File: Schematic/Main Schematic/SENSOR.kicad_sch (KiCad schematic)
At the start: 11 parts, among them IC1 LM75AD,118

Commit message: Updated main schematic but not entirely
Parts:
- renumbered C1 to C9, R1 to R7, R4 to R8, R5 to R9
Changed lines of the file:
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@@
   (symbol (lib_id "power:GND") (at 110.6932 129.2606 0) (unit 1)
     (in_bom yes) (on_board yes) (dnp no) (fields_autoplaced)
-    (property "Reference" "#PWR08" (at 110.6932 135.6106 0)
+    (property "Reference" "#PWR011" (at 110.6932 135.6106 0)
       (effects (font (size 1.27 1.27)) hide)
     )
@@
   (symbol (lib_id "power:GND") (at 87.8332 100.0506 270) (unit 1)
     (in_bom yes) (on_board yes) (dnp no) (fields_autoplaced)
-    (property "Reference" "#PWR05" (at 81.4832 100.0506 0)
+    (property "Reference" "#PWR010" (at 81.4832 100.0506 0)
       (effects (font (size 1.27 1.27)) hide)
     )
@@
   (symbol (lib_id "Device:R") (at 78.9432 109.5756 0) (unit 1)
     (in_bom yes) (on_board yes) (dnp no) (fields_autoplaced)
-    (property "Reference" "R5" (at 81.026 108.9406 0)
+    (property "Reference" "R9" (at 81.026 108.9406 0)
       (effects (font (size 1.27 1.27)) (justify left))
     )
@@
   (symbol (lib_id "power:+3V3") (at 113.1824 92.4306 0) (unit 1)
     (in_bom yes) (on_board yes) (dnp no) (fields_autoplaced)
-    (property "Reference" "#PWR09" (at 113.1824 96.2406 0)
+    (property "Reference" "#PWR012" (at 113.1824 96.2406 0)
       (effects (font (size 1.27 1.27)) hide)
     )
@@
   (symbol (lib_id "Device:R") (at 70.0532 109.5756 0) (unit 1)
     (in_bom yes) (on_board yes) (dnp no) (fields_autoplaced)
-    (property "Reference" "R4" (at 72.5932 108.3055 0)
+    (property "Reference" "R8" (at 72.5932 108.3055 0)
       (effects (font (size 1.27 1.27)) (justify left))
     )
@@
   (symbol (lib_id "Device:R") (at 62.4332 109.5756 0) (unit 1)
     (in_bom yes) (on_board yes) (dnp no) (fields_autoplaced)
-    (property "Reference" "R1" (at 64.9732 108.3055 0)
+    (property "Reference" "R7" (at 64.9732 108.3055 0)
       (effects (font (size 1.27 1.27)) (justify left))
     )
@@
   (symbol (lib_id "pspice:CAP") (at 104.3432 100.0506 90) (unit 1)
     (in_bom yes) (on_board yes) (dnp no) (fields_autoplaced)
-    (property "Reference" "C1" (at 104.3432 91.1606 90)
+    (property "Reference" "C9" (at 104.3432 91.1606 90)
       (effects (font (size 1.27 1.27)))
     )
@@
   (symbol (lib_id "power:GND") (at 85.2932 134.3406 0) (unit 1)
     (in_bom yes) (on_board yes) (dnp no) (fields_autoplaced)
-    (property "Reference" "#PWR01" (at 85.2932 140.6906 0)
-      (effects (font (size 1.27 1.27)) hide)
-    )
+    (property "Reference" "#PWR09" (at 85.2932 140.6906 0)
+      (effects (font (size 1.27 1.27)) hide)
+    )

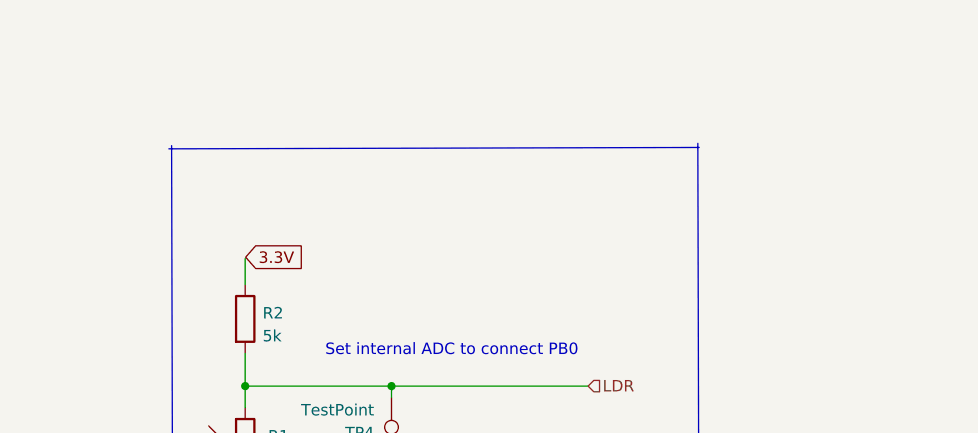
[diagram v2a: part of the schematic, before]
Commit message: I made few comments on the sensing
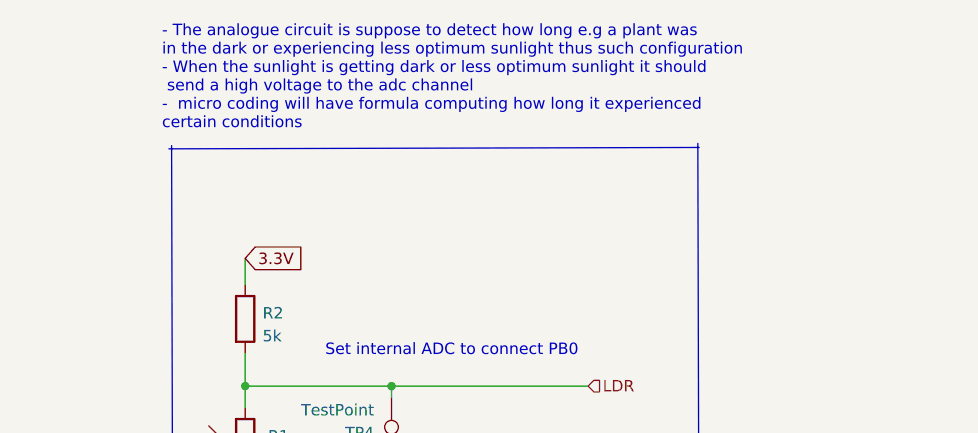
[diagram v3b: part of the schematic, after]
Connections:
- net 3.3V: now also R2.1
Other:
- note added: "- The analogue circuit is suppose to detect how long e.g a plant was in the dark or experiencing less optimum sunlight thus such configuration - When the sunlight is getting dark or less optimum sunlight it should send a high voltage to the adc channel - micro coding will have formula computing how long it experienced certain conditions"
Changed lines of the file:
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@@
     (stroke (width 0) (type default))
+  )
+  (text "- The analogue circuit is suppose to detect how long e.g a plant was \nin the dark or experiencing less optimum sunlight thus such configuration\n- When the sunlight is getting dark or less optimum sunlight it should\n send a high voltage to the adc channel\n-  micro coding will have formula computing how long it experienced \ncertain conditions\n"
+    (at 154.94 83.0072 0)
+    (effects (font (size 1.27 1.27)) (justify left bottom))
   )
   (text "Set internal ADC to connect PB0\n\n" (at 173.0756 110.2614 0)
@@
     (effects (font (size 1.27 1.27)) (justify left bottom))
   )
-  (global_label "3.3V" (shape input) (at 164.2364 97.0534 0)
+  (global_label "3.3V" (shape input) (at 164.1856 97.1804 0)
     (effects (font (size 1.27 1.27)) (justify left))
-    (property "Intersheetrefs" "${INTERSHEET_REFS}" (at 164.2364 97.0534 0)
+    (property "Intersheetrefs" "${INTERSHEET_REFS}" (at 164.1856 97.1804 0)
       (effects (font (size 1.27 1.27)) hide)
     )

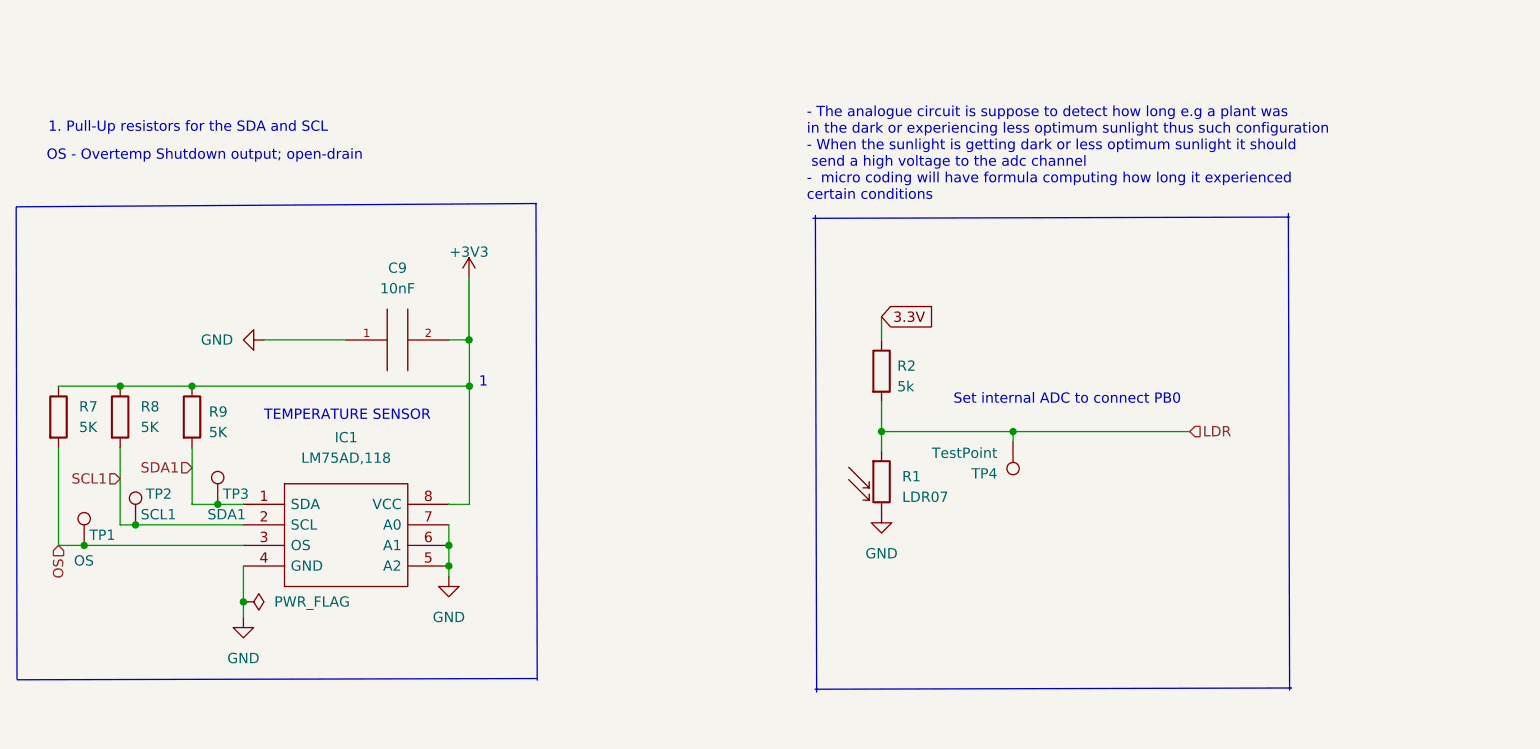
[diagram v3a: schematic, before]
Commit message: I have commented on my module explaining the significant parts
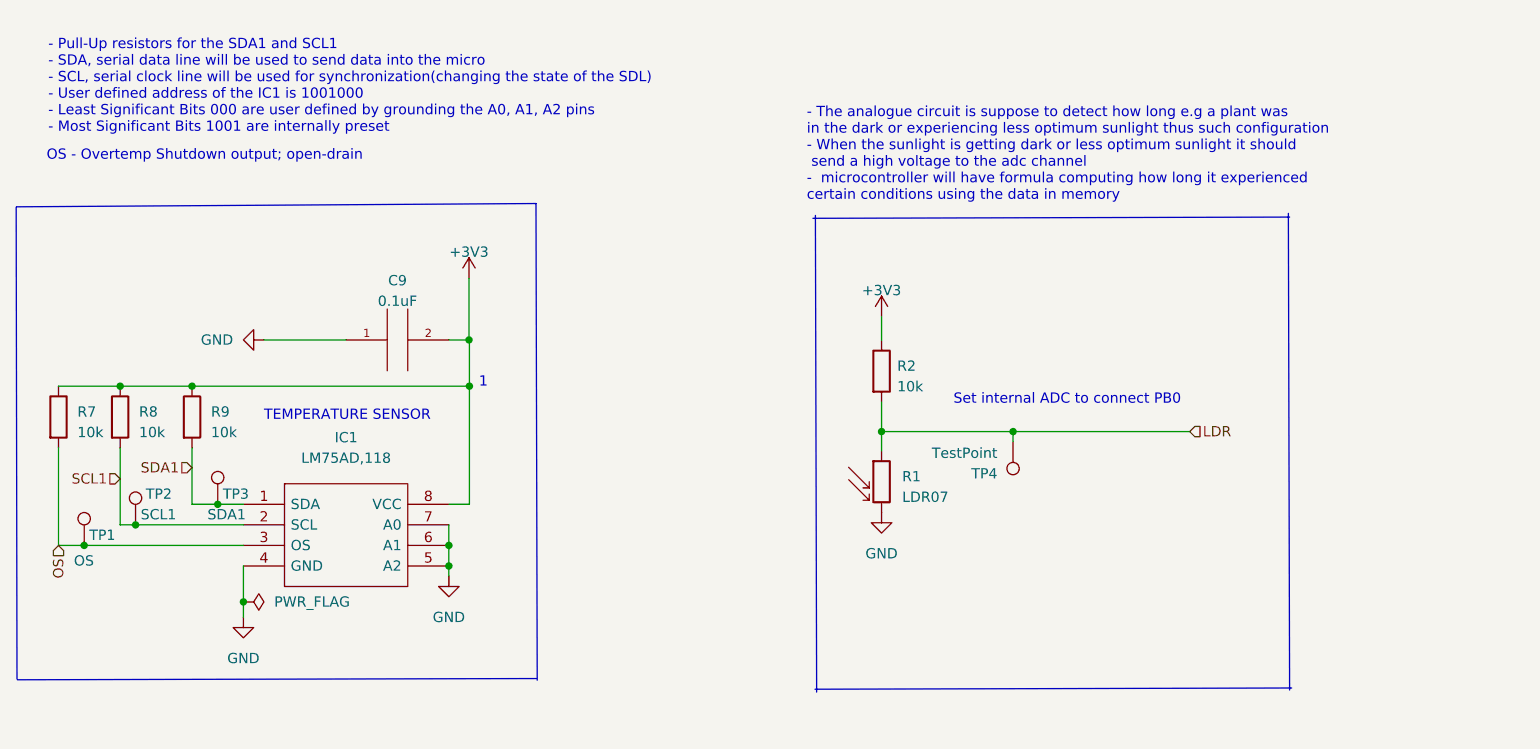
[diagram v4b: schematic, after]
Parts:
- C9: value 10nF -> 0.1uF
- R2: value 5k -> 10k
- R7, R8, R9: value 5K -> 10k
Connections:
- net 3.3V is gone; now on net +3V3: R2.1
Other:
- note added: "- Pull-Up resistors for the SDA1 and SCL1 - SDA, serial data line will be used to send data into the micro - SCL, serial clock line will be used for synchronization(changing the state of the SDL) - User defined address of the IC1 is 1001000 - Least Significant Bits 000 are user defined by grounding the A0, A1, A2 pins - Most Significant Bits 1001 are internally preset"
- note added: "- The analogue circuit is suppose to detect how long e.g a plant was in the dark or experiencing less optimum sunlight thus such configuration - When the sunlight is getting dark or less optimum sunlight it should send a high voltage to the adc channel - microcontroller will have formula computing how long it experienced certain conditions using the data in memory"
- note removed: "- The analogue circuit is suppose to detect how long e.g a plant was in the dark or experiencing less optimum sunlight thus such configuration - When the sunlight is getting dark or less optimum sunlight it should send a high voltage to the adc channel - micro coding will have formula computing how long it experienced certain conditions"
- note removed: "1. Pull-Up resistors for the SDA and SCL"
- company: (none) -> UCT
- title: (none) -> Sensors
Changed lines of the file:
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@@
 (kicad_sch (version 20230121) (generator eeschema)
   (paper "A4")
+  (title_block
+    (title "Sensors")
+    (company "UCT")
+    (comment 4 "Author: Zwivhuya Ndou")
+  )
   (junction (at 164.1856 111.379) (diameter 0) (color 0 0 0 0)
   )
@@
     (stroke (width 0) (type default))
   )
-  (text "- The analogue circuit is suppose to detect how long e.g a plant was \nin the dark or experiencing less optimum sunlight thus such configuration\n- When the sunlight is getting dark or less optimum sunlight it should\n send a high voltage to the adc channel\n-  micro coding will have formula computing how long it experienced \ncertain conditions\n"
+  (text "- The analogue circuit is suppose to detect how long e.g a plant was \nin the dark or experiencing less optimum sunlight thus such configuration\n- When the sunlight is getting dark or less optimum sunlight it should\n send a high voltage to the adc channel\n-  microcontroller will have formula computing how long it experienced \ncertain conditions using the data in memory\n"
     (at 154.94 83.0072 0)
     (effects (font (size 1.27 1.27)) (justify left bottom))
@@
     (effects (font (size 1.27 1.27)) (justify left bottom))
   )
-  (text "1. Pull-Up resistors for the SDA and SCL" (at 61.1632 74.5998 0)
+  (text "- Pull-Up resistors for the SDA1 and SCL1\n- SDA, serial data line will be used to send data into the micro\n- SCL, serial clock line will be used for synchronization(changing the state of the SDL)\n- User defined address of the IC1 is 1001000\n- Least Significant Bits 000 are user defined by grounding the A0, A1, A2 pins\n- Most Significant Bits 1001 are internally preset"
+    (at 61.1632 74.5998 0)
     (effects (font (size 1.27 1.27)) (justify left bottom))
-  )
-  (global_label "3.3V" (shape input) (at 164.1856 97.1804 0)
-    (effects (font (size 1.27 1.27)) (justify left))
-    (property "Intersheetrefs" "${INTERSHEET_REFS}" (at 164.1856 97.1804 0)
-      (effects (font (size 1.27 1.27)) hide)
-    )
   )
   (hierarchical_label "LDR" (shape input) (at 202.2856 111.379 0) (fields_autoplaced)
@@
   (symbol (lib_id "Device:R") (at 78.9432 109.5756 0) (unit 1)
     (in_bom yes) (on_board yes) (dnp no) (fields_autoplaced)
-    (property "Reference" "R9" (at 81.026 108.9406 0)
-      (effects (font (size 1.27 1.27)) (justify left))
-    )
-    (property "Value" "5K" (at 81.026 111.4806 0)
+    (property "Reference" "R9" (at 81.28 108.9406 0)
+      (effects (font (size 1.27 1.27)) (justify left))
+    )
+    (property "Value" "10k" (at 81.28 111.4806 0)
       (effects (font (size 1.27 1.27)) (justify left))
     )
@@
   (symbol (lib_id "Device:R") (at 70.0532 109.5756 0) (unit 1)
     (in_bom yes) (on_board yes) (dnp no) (fields_autoplaced)
-    (property "Reference" "R8" (at 72.5932 108.3055 0)
-      (effects (font (size 1.27 1.27)) (justify left))
-    )
-    (property "Value" "5K" (at 72.5932 110.8455 0)
+    (property "Reference" "R8" (at 72.39 108.9406 0)
+      (effects (font (size 1.27 1.27)) (justify left))
+    )
+    (property "Value" "10k" (at 72.39 111.4806 0)
       (effects (font (size 1.27 1.27)) (justify left))
     )
@@
       (effects (font (size 1.27 1.27)) (justify left))
     )
-    (property "Value" "5k" (at 166.116 105.8164 0)
+    (property "Value" "10k" (at 166.116 105.8164 0)
       (effects (font (size 1.27 1.27)) (justify left))
     )
@@
     )
   )
+  (symbol (lib_id "power:+3V3") (at 164.1856 97.1804 0) (unit 1)
+    (in_bom yes) (on_board yes) (dnp no) (fields_autoplaced)
+    (property "Reference" "#PWR014" (at 164.1856 100.9904 0)
+      (effects (font (size 1.27 1.27)) hide)
+    )
+    (property "Value" "+3V3" (at 164.1856 93.9292 0)
+      (effects (font (size 1.27 1.27)))
+    )
+    (property "Footprint" "" (at 164.1856 97.1804 0)
+      (effects (font (size 1.27 1.27)) hide)
+    )
+    (property "Datasheet" "" (at 164.1856 97.1804 0)
+      (effects (font (size 1.27 1.27)) hide)
+    )
+    (pin "1")
+    (instances
+      (project "Main Schematic"
+        (path "/81c41bad-bb43-41af-b405-18d135a809b1/820a1ce6-42c1-4792-8ad0-5e2a5c074ed4"
+          (reference "#PWR014") (unit 1)
+        )
+      )
+    )
+  )
   (symbol (lib_id "power:GND") (at 164.1856 121.3866 0) (unit 1)
     (in_bom yes) (on_board yes) (dnp no) (fields_autoplaced)
@@
   (symbol (lib_id "Device:R") (at 62.4332 109.5756 0) (unit 1)
     (in_bom yes) (on_board yes) (dnp no) (fields_autoplaced)
-    (property "Reference" "R7" (at 64.9732 108.3055 0)
-      (effects (font (size 1.27 1.27)) (justify left))
-    )
-    (property "Value" "5K" (at 64.9732 110.8455 0)
+    (property "Reference" "R7" (at 64.77 108.9406 0)
+      (effects (font (size 1.27 1.27)) (justify left))
+    )
+    (property "Value" "10k" (at 64.77 111.4806 0)
       (effects (font (size 1.27 1.27)) (justify left))
     )
@@
   (symbol (lib_id "pspice:CAP") (at 104.3432 100.0506 90) (unit 1)
     (in_bom yes) (on_board yes) (dnp no) (fields_autoplaced)
-    (property "Reference" "C9" (at 104.3432 91.1606 90)
-      (effects (font (size 1.27 1.27)))
-    )
-    (property "Value" "10nF" (at 104.3432 93.7006 90)
-      (effects (font (size 1.27 1.27)))
-    )
+    (property "Reference" "C9" (at 104.3432 92.71 90)
+      (effects (font (size 1.27 1.27)))
+    )
+    (property "Value" "0.1uF" (at 104.3432 95.25 90)
+      (effects (font (size 1.27 1.27)))
+    )

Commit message: Sensor comment
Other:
- note added: "- Pull-Up resistors for the SDA1 and SCL1 - SDA, serial data line will be used to send data into the micro - SCL, serial clock line will be used for synchronization(changing the state of the SDL) - User defined address of the IC1 is 1001000 - Least Significant Bits 000 are user defined by grounding the A0, A1, A2 pins - Most Significant Bits 1001 are internally preset - OS - Overtemp Shutdown out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"
- note removed: "- Pull-Up resistors for the SDA1 and SCL1 - SDA, serial data line will be used to send data into the micro - SCL, serial clock line will be used for synchronization(changing the state of the SDL) - User defined address of the IC1 is 1001000 - Least Significant Bits 000 are user defined by grounding the A0, A1, A2 pins - Most Significant Bits 1001 are internally preset"
- note removed: "OS - Overtemp Shutdown output; open-drain"
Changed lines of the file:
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@@
     (effects (font (size 1.27 1.27)) (justify left bottom))
   )
-  (text "OS - Overtemp Shutdown output; open-drain" (at 60.96 78.0542 0)
-    (effects (font (size 1.27 1.27)) (justify left bottom))
-  )
-  (text "- Pull-Up resistors for the SDA1 and SCL1\n- SDA, serial data line will be used to send data into the micro\n- SCL, serial clock line will be used for synchronization(changing the state of the SDL)\n- User defined address of the IC1 is 1001000\n- Least Significant Bits 000 are user defined by grounding the A0, A1, A2 pins\n- Most Significant Bits 1001 are internally preset"
+  (text "- Pull-Up resistors for the SDA1 and SCL1\n- SDA, serial data line will be used to send data into the micro\n- SCL, serial clock line will be used for synchronization(changing the state of the SDL)\n- User defined address of the IC1 is 1001000\n- Least Significant Bits 000 are user defined by grounding the A0, A1, A2 pins\n- Most Significant Bits 1001 are internally preset\n- OS - Overtemp Shutdown output; open-drain"
     (at 61.1632 74.5998 0)
     (effects (font (size 1.27 1.27)) (justify left bottom))

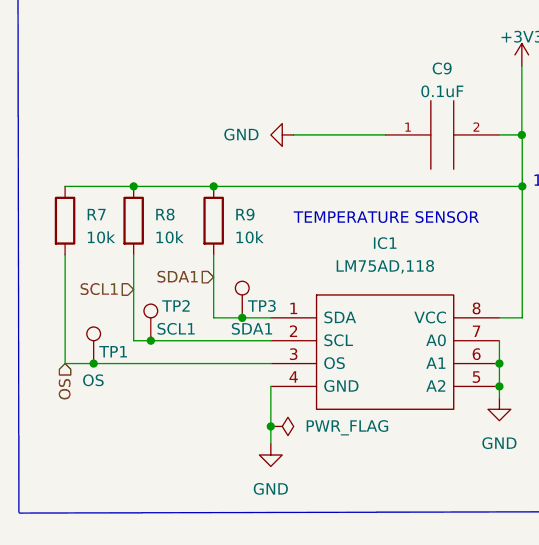
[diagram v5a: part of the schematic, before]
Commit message: I have added net lables and hierachy labels on the main schmeatic
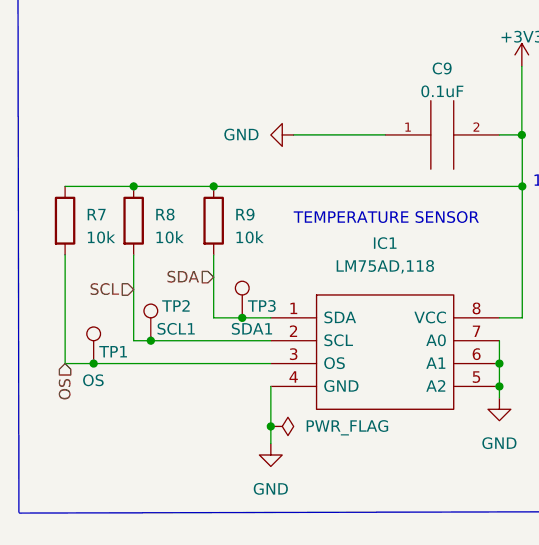
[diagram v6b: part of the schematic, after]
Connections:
- net SCL1 renamed SCL
- net SDA1 renamed SDA
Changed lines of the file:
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@@
     (effects (font (size 1.27 1.27)) (justify right))
   )
-  (hierarchical_label "SDA1" (shape input) (at 78.9432 115.8494 180) (fields_autoplaced)
+  (hierarchical_label "SDA" (shape input) (at 78.9432 115.8494 180) (fields_autoplaced)
     (effects (font (size 1.27 1.27)) (justify right))
   )
-  (hierarchical_label "SCL1" (shape input) (at 70.0532 117.221 180) (fields_autoplaced)
+  (hierarchical_label "SCL" (shape input) (at 70.0532 117.221 180) (fields_autoplaced)
     (effects (font (size 1.27 1.27)) (justify right))
   )
